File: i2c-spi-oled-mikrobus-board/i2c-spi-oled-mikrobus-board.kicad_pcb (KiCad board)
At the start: 4 copper layers, 25.4 x 42.9 mm, 10 parts, among them J1 mikroBUS_L, J2 mikroBUS_R, J3 Conn_02x08_Odd_Even, U1 SC18IS606PW, U2 PCA9557PW

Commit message: i2c-spi-oled: also connect the R/~W pin
the display doesn't need it (it will be held to GND) but we might reuse
this board for other SPI components
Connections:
- J3 pad 1: GND -> /D_R_~{W}
- U2 pad 10: unconnected-(U2-Pad10) -> /D_R_~{W}
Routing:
- net /D_R_~{W}: track 0.00 -> 41.2 mm, vias 0 -> 4
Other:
- rule pad_to_mask_clearance: 0 -> 0.05
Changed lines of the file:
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@@
 (kicad_pcb (version 20211014) (generator pcbnew)
   (general
-    (thickness 4.69)
+    (thickness 1.6062)
   )
   (paper "A4")
@@
       (layer "F.Mask" (type "Top Solder Mask") (thickness 0.01))
       (layer "F.Cu" (type "copper") (thickness 0.035))
-      (layer "dielectric 1" (type "core") (thickness 1.51) (material "FR4") (epsilon_r 4.5) (loss_tangent 0.02))
-      (layer "In1.Cu" (type "copper") (thickness 0.035))
-      (layer "dielectric 2" (type "prepreg") (thickness 1.51) (material "FR4") (epsilon_r 4.5) (loss_tangent 0.02))
-      (layer "In2.Cu" (type "copper") (thickness 0.035))
-      (layer "dielectric 3" (type "core") (thickness 1.51) (material "FR4") (epsilon_r 4.5) (loss_tangent 0.02))
+      (layer "dielectric 1" (type "core") (thickness 0.2104) (material "FR4") (epsilon_r 4.5) (loss_tangent 0.02))
+      (layer "In1.Cu" (type "copper") (thickness 0.0152))
+      (layer "dielectric 2" (type "prepreg") (thickness 1.065) (material "FR4") (epsilon_r 4.5) (loss_tangent 0.02))
+      (layer "In2.Cu" (type "copper") (thickness 0.0152))
+      (layer "dielectric 3" (type "core") (thickness 0.2104) (material "FR4") (epsilon_r 4.5) (loss_tangent 0.02))
       (layer "B.Cu" (type "copper") (thickness 0.035))
-      (layer "B.Mask" (type "Bottom Solder Mask") (thickness 0.01))
+      (layer "B.Mask" (type "Bottom Solder Mask") (color "#808080D4") (thickness 0.01))
       (layer "B.Paste" (type "Bottom Solder Paste"))
       (layer "B.SilkS" (type "Bottom Silk Screen"))
-      (copper_finish "None")
+      (copper_finish "HAL lead-free")
       (dielectric_constraints no)
     )
-    (pad_to_mask_clearance 0)
+    (pad_to_mask_clearance 0.05)
+    (solder_mask_min_width 0.2)
     (pcbplotparams
       (layerselection 0x00010fc_ffffffff)
@@
   (net 31 "unconnected-(U1-Pad8)")
   (net 32 "unconnected-(U1-Pad16)")
-  (net 33 "unconnected-(U2-Pad10)")
+  (net 33 "/D_R_~{W}")
   (net 34 "unconnected-(U2-Pad11)")
   (net 35 "unconnected-(U2-Pad12)")
   (net 36 "unconnected-(U2-Pad13)")
   (net 37 "unconnected-(U2-Pad14)")
-  (net 38 "Net-(R1-Pad2)")
+  (net 38 "Net-(LD1-Pad2)")
   (footprint "Capacitor_SMD:C_0402_1005Metric" (layer "F.Cu")
     (at 39.624 41.91 -90)
@@
       (net 1 "GND") (pinfunction "K") (pintype "passive"))
     (pad "2" smd roundrect (at 0.7875 0 180) (size 0.875 0.95) (layers "F.Cu" "F.Paste" "F.Mask") (roundrect_rratio 0.25)
-      (net 38 "Net-(R1-Pad2)") (pinfunction "A") (pintype "passive"))
+      (net 38 "Net-(LD1-Pad2)") (pinfunction "A") (pintype "passive"))
     (model "${KICAD6_3DMODEL_DIR}/LED_SMD.3dshapes/LED_0603_1608Metric.wrl"
       (offset (xyz 0 0 0))
@@
       (net 17 "/D_EN") (pinfunction "IO2") (pintype "bidirectional"))
     (pad "10" smd roundrect (at 2.8625 1.625 90) (size 1.475 0.4) (layers "F.Cu" "F.Paste" "F.Mask") (roundrect_rratio 0.25)
-      (net 33 "unconnected-(U2-Pad10)") (pinfunction "IO3") (pintype "bidirectional+no_connect"))
+      (net 33 "/D_R_~{W}") (pinfunction "IO3") (pintype "bidirectional"))
     (pad "11" smd roundrect (at 2.8625 0.975 90) (size 1.475 0.4) (layers "F.Cu" "F.Paste" "F.Mask") (roundrect_rratio 0.25)
       (net 34 "unconnected-(U2-Pad11)") (pinfunction "IO4") (pintype "bidirectional+no_connect"))
@@
     (fp_rect (start 2.975 0.435) (end 3.375 2.75) (layer "F.Fab") (width 0.1) (fill none))
     (pad "1" smd rect (at -4.445 2.02) (size 0.65 2.76) (layers "F.Cu" "F.Paste" "F.Mask")
-      (net 1 "GND") (pinfunction "Pin_1") (pintype "passive"))
+      (net 33 "/D_R_~{W}") (pinfunction "Pin_1") (pintype "passive"))
     (pad "2" smd rect (at -4.445 -2.02) (size 0.65 2.76) (layers "F.Cu" "F.Paste" "F.Mask")
       (net 16 "/D_D_~{C}") (pinfunction "Pin_2") (pintype "passive"))
@@
       (net 2 "+3.3V") (pintype "passive"))
     (pad "2" smd roundrect (at 0.825 0) (size 0.8 0.95) (layers "F.Cu" "F.Paste" "F.Mask") (roundrect_rratio 0.25)
-      (net 38 "Net-(R1-Pad2)") (pintype "passive"))
+      (net 38 "Net-(LD1-Pad2)") (pintype "passive"))
     (model "${KICAD6_3DMODEL_DIR}/Resistor_SMD.3dshapes/R_0603_1608Metric.wrl"
       (offset (xyz 0 0 0))
@@
   (segment (start 41.402 50.292) (end 43.434 52.324) (width 0.8) (layer "In1.Cu") (net 30))
   (segment (start 36.068 50.292) (end 41.402 50.292) (width 0.8) (layer "In1.Cu") (net 30))
+  (segment (start 43.535 45.821) (end 43.688 45.974) (width 0.4) (layer "F.Cu") (net 33))
+  (segment (start 33.655 34.913) (end 28.563 34.913) (width 0.65) (layer "F.Cu") (net 33))
+  (segment (start 43.535 44.0005) (end 43.535 45.821) (width 0.4) (layer "F.Cu") (net 33))
+  (segment (start 28.563 34.913) (end 28.448 34.798) (width 0.65) (layer "F.Cu") (net 33))
+  (via (at 43.688 45.974) (size 0.8) (drill 0.4) (layers "F.Cu" "B.Cu") (net 33))
+  (via (at 47.752 34.798) (size 0.8) (drill 0.4) (layers "F.Cu" "B.Cu") (net 33))
+  (via (at 47.752 44.958) (size 0.8) (drill 0.4) (layers "F.Cu" "B.Cu") (net 33))
+  (via (at 28.448 34.798) (size 0.8) (drill 0.4) (layers "F.Cu" "B.Cu") (net 33))
+  (segment (start 47.752 34.798) (end 47.752 44.958) (width 0.8) (layer "In1.Cu") (net 33))
+  (segment (start 43.688 45.974) (end 46.736 45.974) (width 0.8) (layer "In2.Cu") (net 33))
+  (segment (start 46.736 45.974) (end 47.752 44.958) (width 0.8) (layer "In2.Cu") (net 33))
+  (segment (start 28.448 34.798) (end 47.752 34.798) (width 0.8) (layer "In2.Cu") (net 33))
   (segment (start 36.131 65.405) (end 39.624 65.405) (width 0.8) (layer "F.Cu") (net 38))
   (zone (net 1) (net_name "GND") (layer "F.Cu") (hatch edge 0.508)

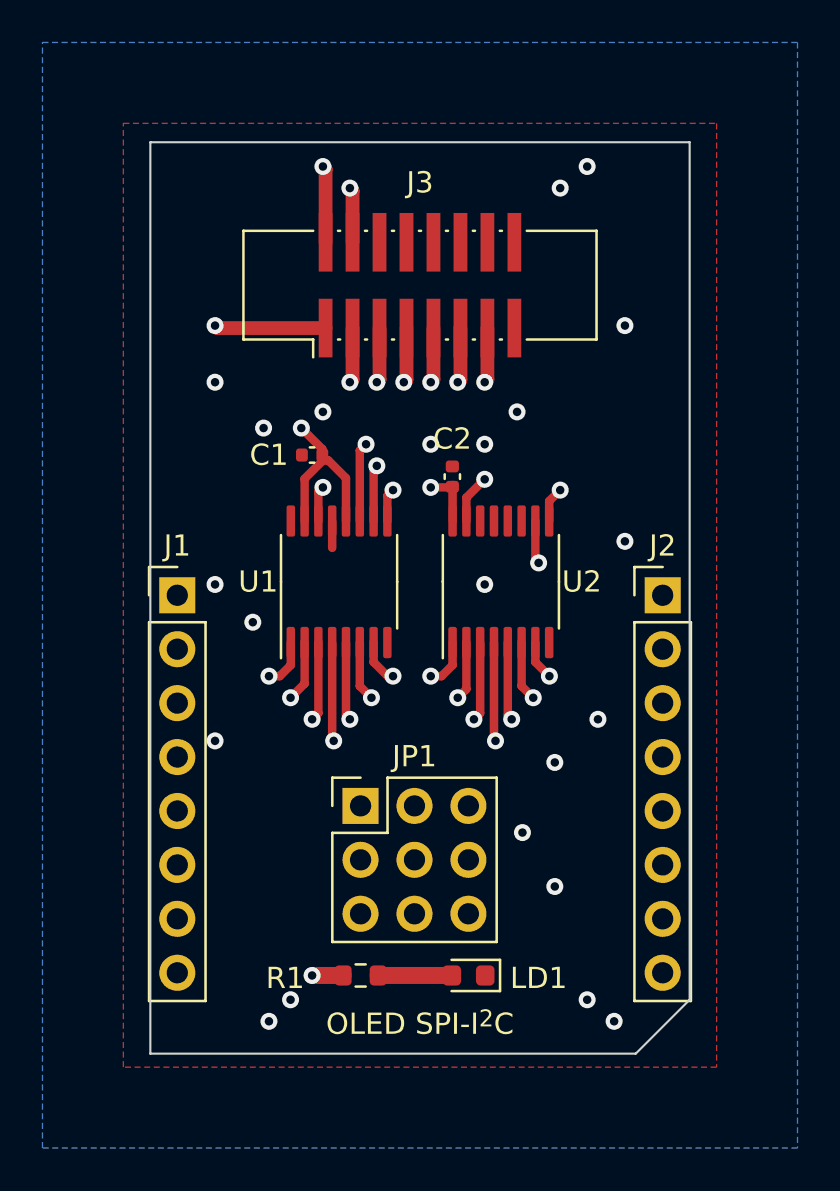
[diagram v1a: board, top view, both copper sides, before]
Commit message: oled: add JLCPCB mounting holes
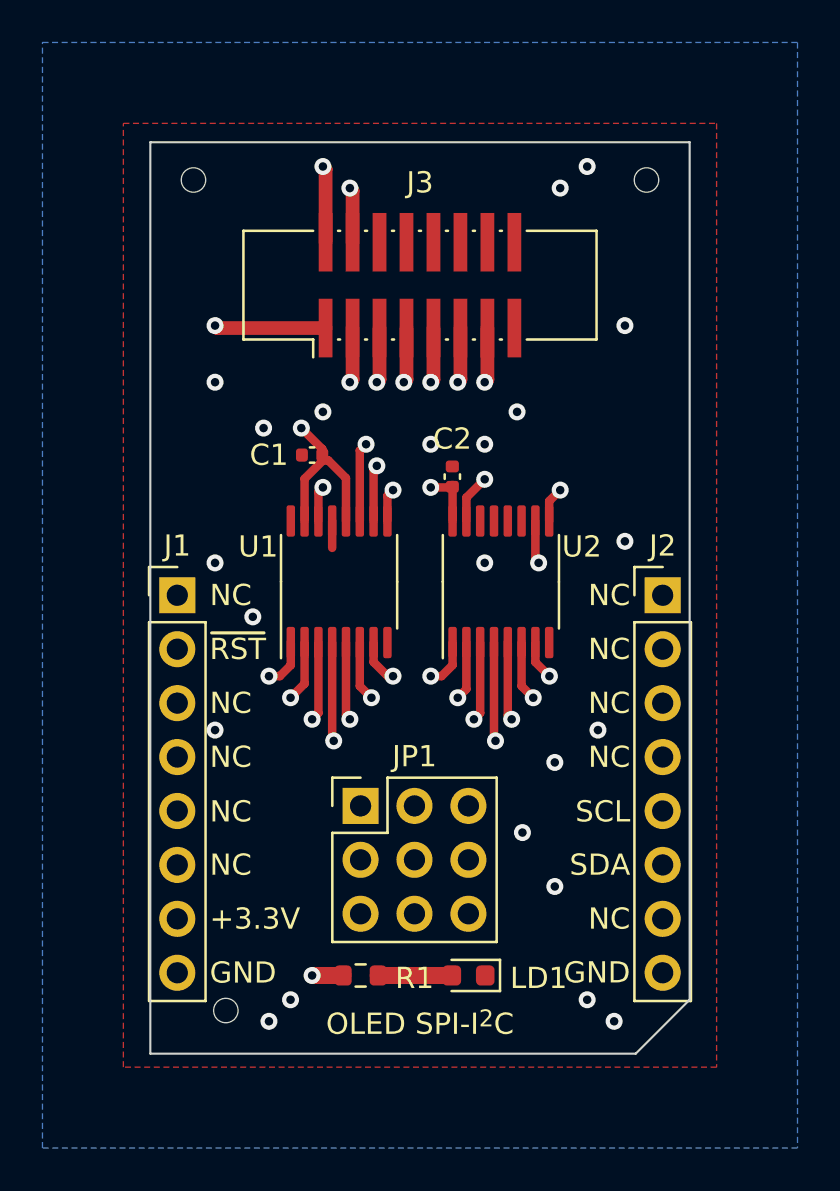
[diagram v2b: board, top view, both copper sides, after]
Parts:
- added REF**: JLCPCB_Mounting_Hole, JLCPCB:JLCPCB_Mounting_Hole, F.Cu at (29.0, 67.1)
- added REF**: JLCPCB_Mounting_Hole, JLCPCB:JLCPCB_Mounting_Hole, F.Cu at (27.4, 27.9)
- added REF**: JLCPCB_Mounting_Hole, JLCPCB:JLCPCB_Mounting_Hole, F.Cu at (48.8, 27.9)
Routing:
- net /~{RST}: track 57.8 -> 56.4 mm
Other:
- board text added: "+3.3V"
- board text added: "GND"
- board text added: "NC"
- board text added: "SCL"
- board text added: "SDA"
- board text added: "~{RST}"

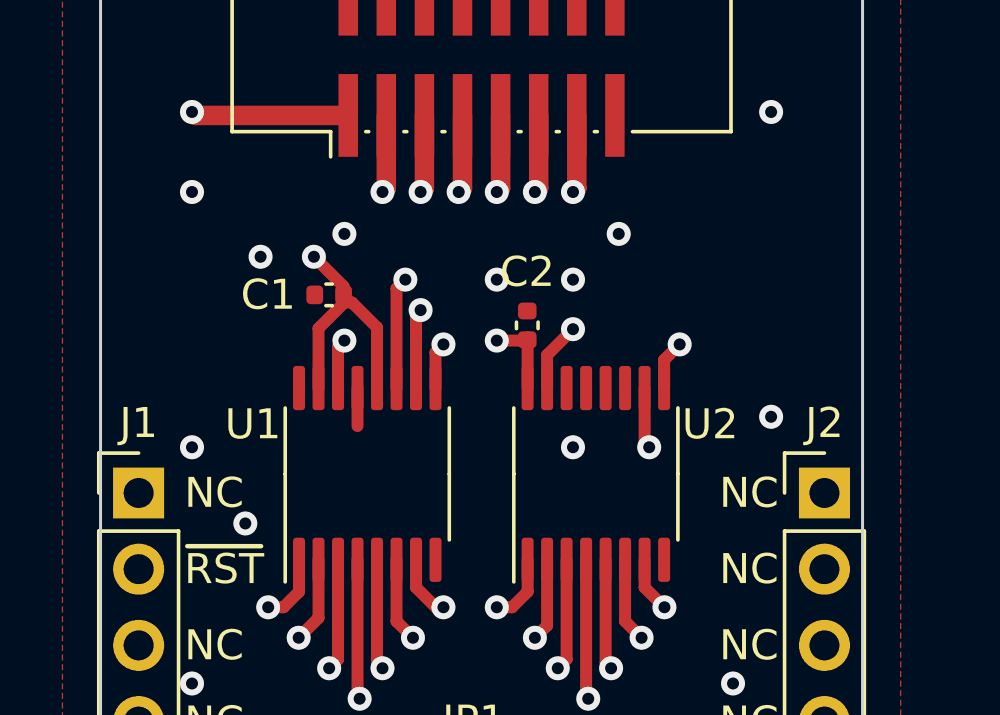
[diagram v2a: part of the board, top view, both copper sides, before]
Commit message: i2c-spi-oled: put ~RST signal on port expander too
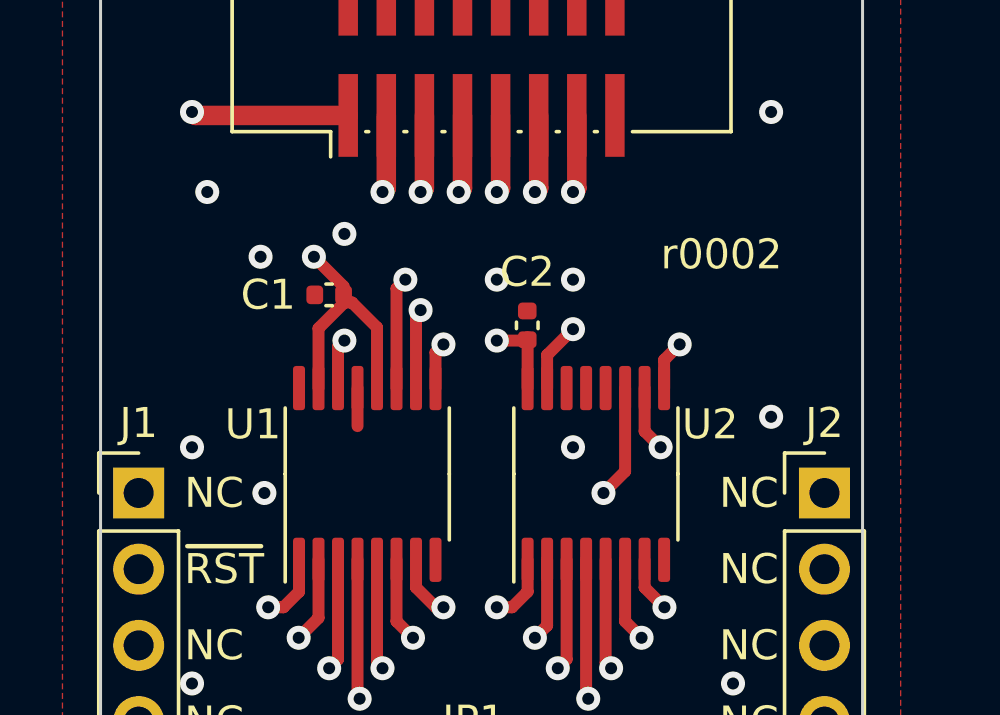
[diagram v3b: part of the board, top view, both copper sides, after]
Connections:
- J3 pad 3: /~{RST} -> /D_~{RST}
- U2 pad 11: unconnected-(U2-Pad11) -> /D_~{RST}
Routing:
- net /D_~{RST}: track 0.00 -> 34.4 mm, vias 0 -> 4
- net /~{RST}: track 56.4 -> 39.0 mm, vias 7 -> 5
- net GND: vias 2 -> 1
- net +3.3V: vias 6 -> 5
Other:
- board text added: "r0002"
